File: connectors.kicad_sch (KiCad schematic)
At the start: 9 parts, among them J7001 PinHeader_1x3_P2.54mm_SMD, J7002 PinHeader_1x3_P2.54mm_SMD, J7003 Tag-Connect_TC2050-IDC-NL_2x5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

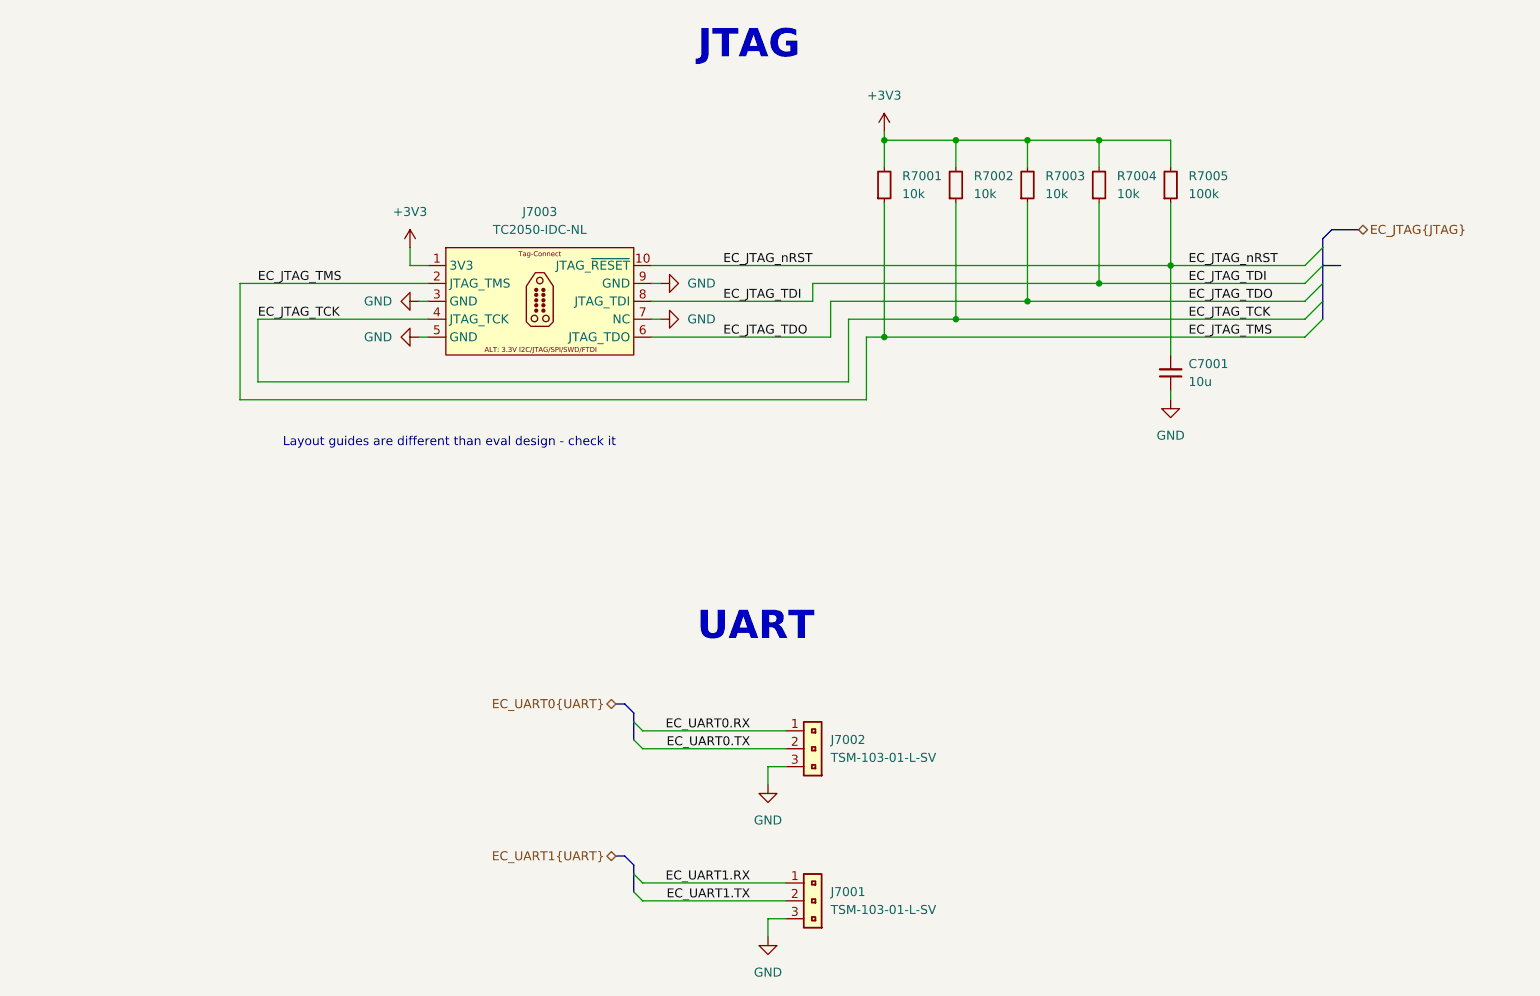
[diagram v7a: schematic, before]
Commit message: [#103224] connectors: fix JTAG bus
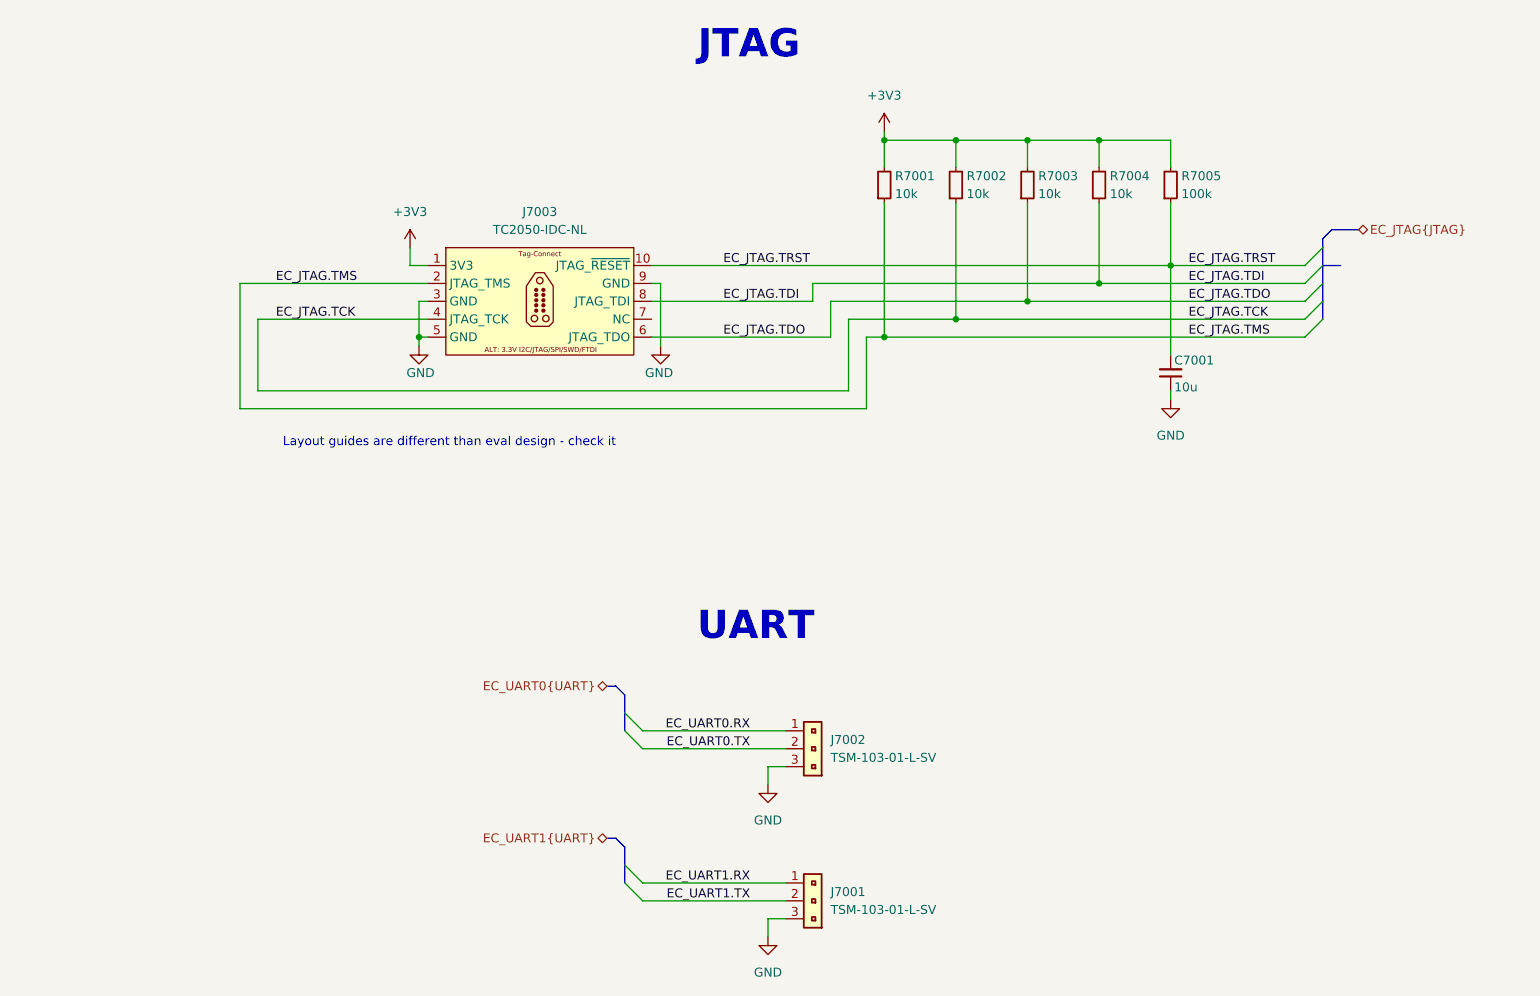
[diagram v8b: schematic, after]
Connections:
- net GND: no longer J7003.7
- net EC_JTAG_TCK renamed EC_JTAG.TCK
- net EC_JTAG_TDI renamed EC_JTAG.TDI
- net EC_JTAG_TDO renamed EC_JTAG.TDO
- net EC_JTAG_TMS renamed EC_JTAG.TMS
- net EC_JTAG_nRST renamed EC_JTAG.TRST
